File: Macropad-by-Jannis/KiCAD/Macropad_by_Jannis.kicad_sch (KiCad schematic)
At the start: 7 parts, among them SW1 SW_Push, SW2 SW_Push, SW3 SW_Push, SW4 SW_Push, U1 XIAO-RP2040-DIP

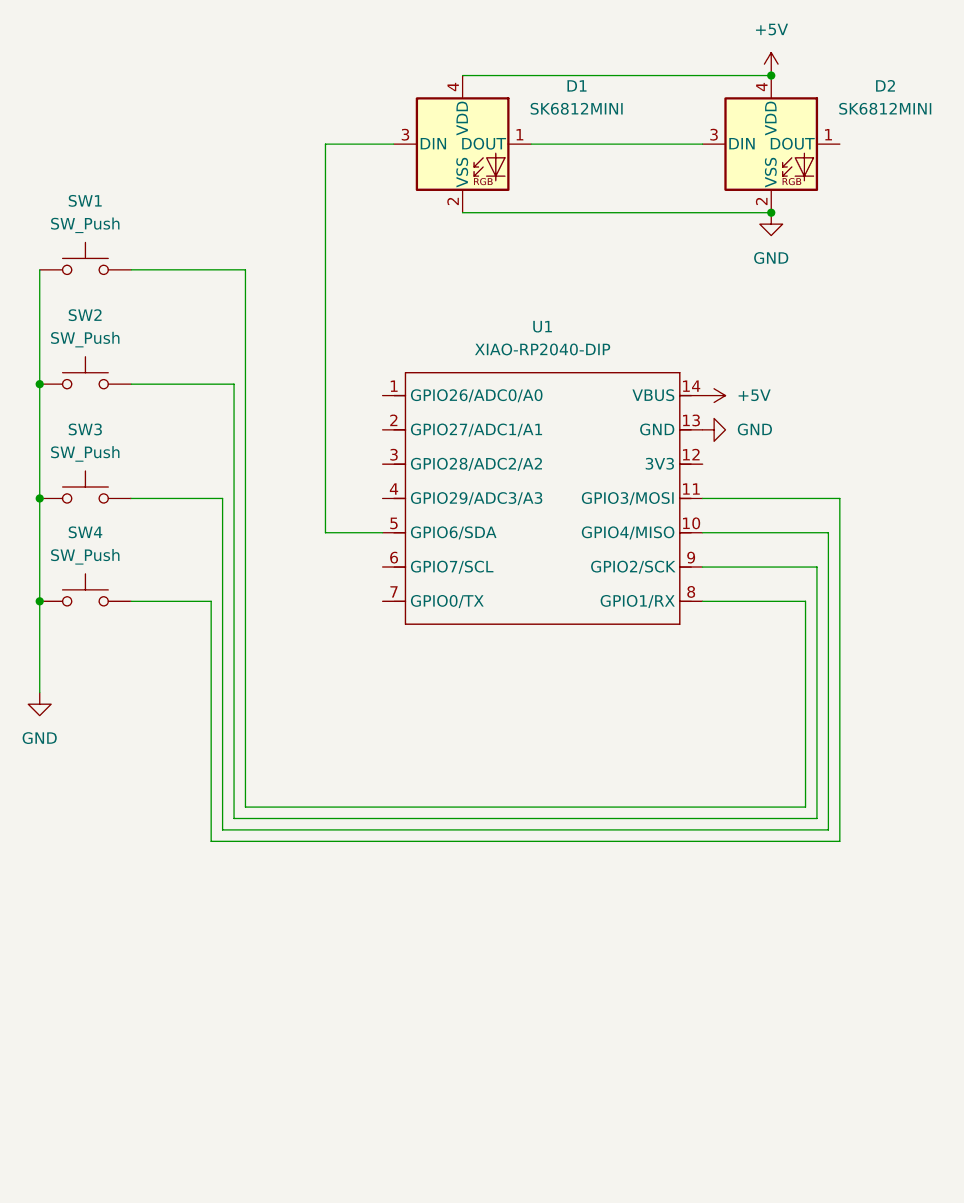
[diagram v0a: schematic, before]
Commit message: 3 reihen
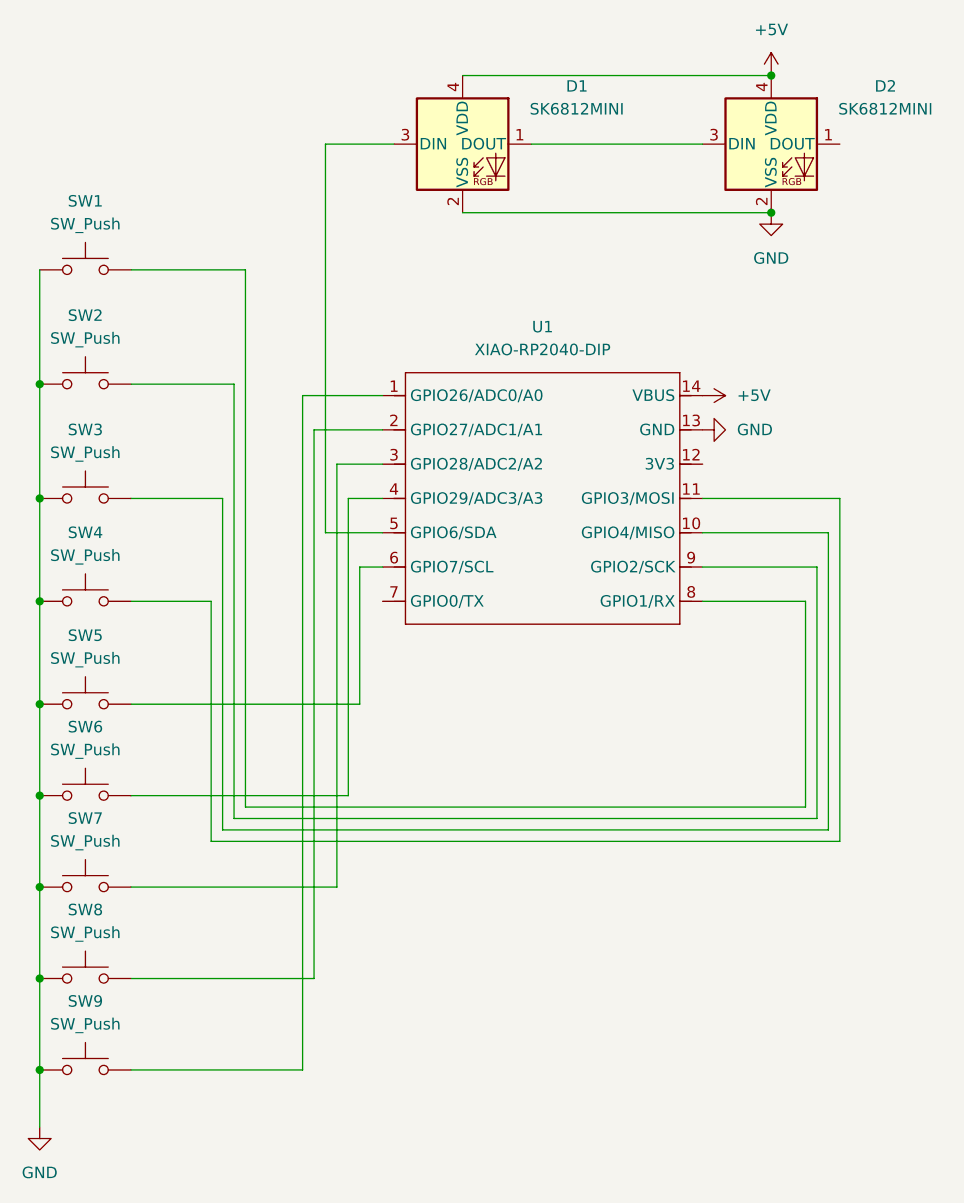
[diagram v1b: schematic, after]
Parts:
- added SW5, SW6, SW7, SW8, SW9: SW_Push, Button_Switch_Keyboard:SW_Cherry_MX_1.00u_Plate, symbol Switch:SW_Push
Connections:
- net GND: now also SW5.1, SW6.1, SW7.1, SW8.1, SW9.1
- net at U1.1 (GPIO26/ADC0/A0): now also SW9.2
- net at U1.2 (GPIO27/ADC1/A1): now also SW8.2
- net at U1.3 (GPIO28/ADC2/A2): now also SW7.2
- net at U1.4 (GPIO29/ADC3/A3): now also SW6.2
- net at U1.6 (GPIO7/SCL): now also SW5.2
